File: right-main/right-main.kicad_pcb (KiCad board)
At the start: 2 copper layers, 150.4 x 123.8 mm, 208 parts, among them J1 USBCONN, P1 CONN_4, P2 CONN_5, P3 CONN_6, SW1 PTS525SM10, SW11 SPST, SW12 SPST, SW13 SPST, SW14 SPST, SW15 SPST, SW16 SPST, SW17 SPST, SW21 SPST, SW22 SPST, SW23 SPST, SW24 SPST, SW25 SPST, SW26 SPST, SW27 SPST, SW31 SPST, SW32 SPST, SW33 SPST, SW34 SPST, SW35 SPST, SW36 SPST, SW37 SPST, SW41 SPST, SW42 SPST, SW43 SPST, SW44 SPST, SW45 SPST, SW46 SPST, SW47 SPST, SW52 SPST, SW53 SPST, SW54 SPST, SW55 SPST, SW56 SPST, SW57 SPST, U1 ATMEGA32U4, U2 CAT24C256, X1 16Mhz

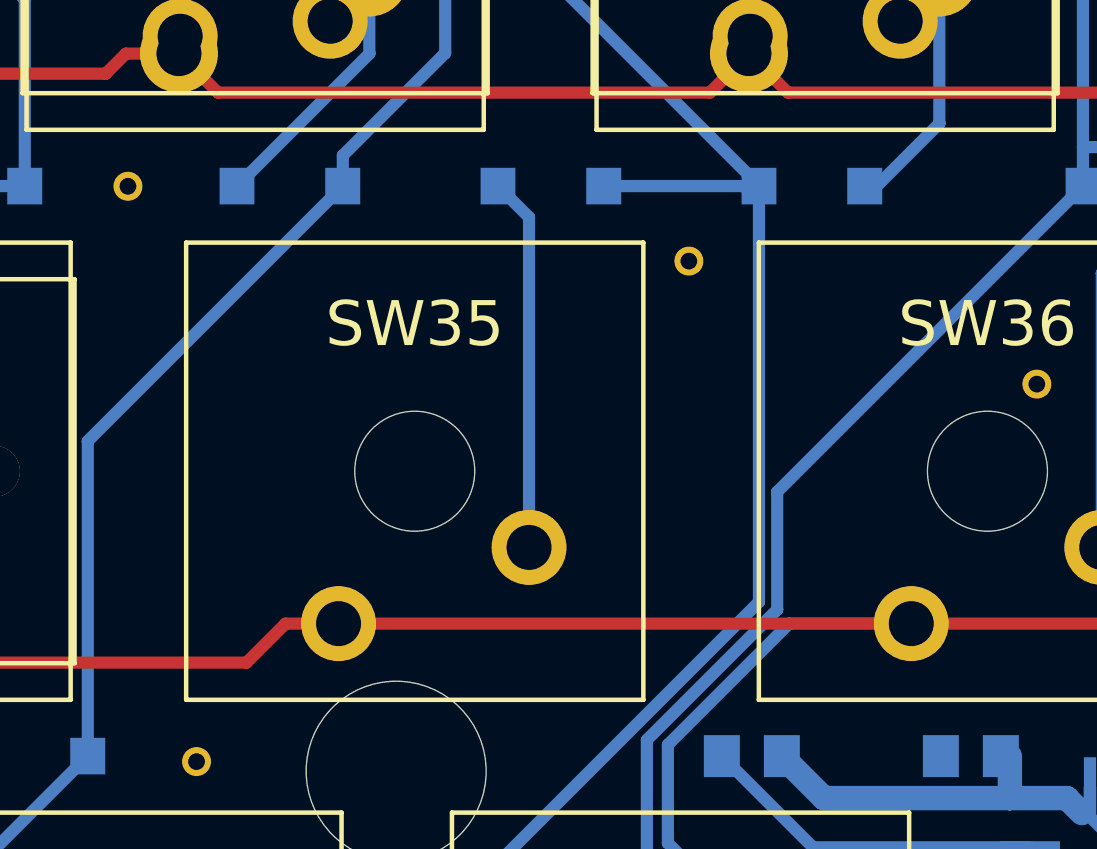
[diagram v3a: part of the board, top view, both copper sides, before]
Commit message: switch 35 right
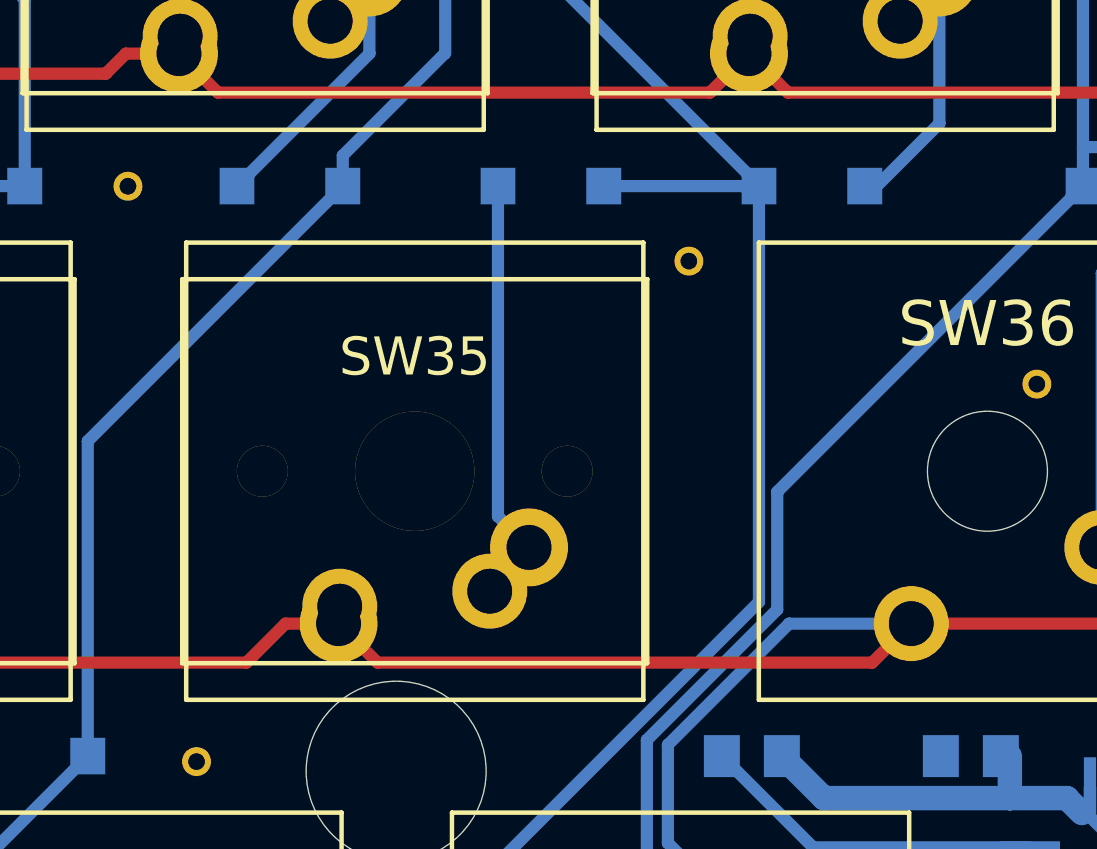
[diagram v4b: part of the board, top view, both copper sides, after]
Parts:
- SW35: footprint UGL:Cherry_MX -> ugl:Cherry-MX-Matias-Hybrid
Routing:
- net Net-(D35-Pad2): track 13.5 -> 15.5 mm
- net /ROW3: track 190.5 -> 191.6 mm
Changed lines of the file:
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@@
 (kicad_pcb (version 4) (host pcbnew 4.0.1-stable)
   (general
-    (links 345)
-    (no_connects 3)
+    (links 347)
+    (no_connects 0)
     (area 19.803 18.9051 270.000001 165.000001)
     (thickness 1.6)
     (drawings 354)
-    (tracks 1050)
+    (tracks 1054)
     (zones 0)
     (modules 208)
@@
   (layers
     (0 F.Cu signal)
-    (31 B.Cu signal hide)
+    (31 B.Cu signal)
     (32 B.Adhes user)
     (33 F.Adhes user)
@@
       (net 18 /ROW3))
   )
-  (module UGL:Cherry_MX locked (layer F.Cu)
-    (at 197.52 101.7 180)
-    (fp_text reference SW35 (at 0 4.9 180) (layer F.SilkS)
-      (effects (font (size 1.5 1.5) (thickness 0.3)))
-    )
-    (fp_text value SPST (at 0 0 180) (layer F.SilkS) hide
-      (effects (font (size 1.5 1.5) (thickness 0.3)))
-    )
-    (fp_line (start -7.6 -7.6) (end -7.6 7.6) (layer B.SilkS) (width 0.15))
-    (fp_line (start -7.6 7.6) (end 7.6 7.6) (layer B.SilkS) (width 0.15))
-    (fp_line (start 7.6 -7.6) (end 7.6 7.6) (layer B.SilkS) (width 0.15))
-    (fp_line (start -7.6 -7.6) (end 7.6 -7.6) (layer B.SilkS) (width 0.15))
-    (fp_line (start -7.62 -7.62) (end 7.62 -7.62) (layer F.SilkS) (width 0.15))
-    (fp_line (start 7.62 -7.62) (end 7.62 7.62) (layer F.SilkS) (width 0.15))
-    (fp_line (start 7.62 7.62) (end -7.62 7.62) (layer F.SilkS) (width 0.15))
-    (fp_line (start -7.62 7.62) (end -7.62 -7.62) (layer F.SilkS) (width 0.15))
-    (pad "" np_thru_hole circle (at 0 0 180) (size 4 4) (drill 4) (layers *.Cu *.Mask F.SilkS))
-    (pad 2 thru_hole circle (at -3.81 -2.54 180) (size 2.5 2.5) (drill 1.5) (layers *.Cu *.Mask F.SilkS)
-      (net 48 "Net-(D35-Pad2)"))
-    (pad 1 thru_hole circle (at 2.54 -5.08 180) (size 2.5 2.5) (drill 1.5) (layers *.Cu *.Mask F.SilkS)
-      (net 18 /ROW3))
-  )
   (module UGL:UX60-MB-5S8 locked (layer F.Cu)
     (at 175.849803 43.601924 85.4)
@@
     )
   )
+  (module ugl:Cherry-MX-Matias-Hybrid locked (layer F.Cu)
+    (at 197.52 101.7 180)
+    (tags switch)
+    (fp_text reference SW35 (at 0 3.81 180) (layer F.SilkS)
+      (effects (font (thickness 0.3048)))
+    )
+    (fp_text value SPST (at 0 0 180) (layer F.SilkS) hide
+      (effects (font (thickness 0.3048)))
+    )
+    (fp_line (start -7.62 7.62) (end -7.62 -7.62) (layer B.SilkS) (width 0.15))
+    (fp_line (start 7.62 7.62) (end -7.62 7.62) (layer B.SilkS) (width 0.15))
+    (fp_line (start 7.62 -7.62) (end 7.62 7.62) (layer B.SilkS) (width 0.15))
+    (fp_line (start -7.62 -7.62) (end 7.62 -7.62) (layer B.SilkS) (width 0.15))
+    (fp_line (start -7.75 -6.4) (end -7.75 6.4) (layer F.SilkS) (width 0.15))
+    (fp_line (start 7.75 -6.4) (end 7.75 6.4) (layer F.SilkS) (width 0.15))
+    (fp_line (start -7.75 6.4) (end 7.75 6.4) (layer F.SilkS) (width 0.15))
+    (fp_line (start -7.75 -6.4) (end 7.75 -6.4) (layer F.SilkS) (width 0.15))
+    (fp_line (start -7.62 -7.62) (end 7.62 -7.62) (layer F.SilkS) (width 0.15))
+    (fp_line (start 7.62 -7.62) (end 7.62 7.62) (layer F.SilkS) (width 0.15))
+    (fp_line (start 7.62 7.62) (end -7.62 7.62) (layer F.SilkS) (width 0.15))
+    (fp_line (start -7.62 7.62) (end -7.62 -7.62) (layer F.SilkS) (width 0.15))
+    (pad 0 thru_hole circle (at 0 0 180) (size 3.98018 3.98018) (drill 3.98018) (layers *.Cu *.Mask F.SilkS))
+    (pad 1 thru_hole circle (at 2.54 -5.08 180) (size 2.6 2.6) (drill 1.5011) (layers *.Cu *.Mask F.SilkS)
+      (net 18 /ROW3))
+    (pad 2 thru_hole circle (at -3.81 -2.54 180) (size 2.6 2.6) (drill 1.5011) (layers *.Cu *.Mask F.SilkS)
+      (net 48 "Net-(D35-Pad2)"))
+    (pad "" thru_hole circle (at -5.08 0 180) (size 1.69926 1.69926) (drill 1.69926) (layers *.Cu *.Mask F.SilkS))
+    (pad "" thru_hole circle (at 5.08 0 180) (size 1.69926 1.69926) (drill 1.69926) (layers *.Cu *.Mask F.SilkS))
+    (pad 1 thru_hole circle (at 2.5 -4.5 180) (size 2.5 2.5) (drill 1.5) (layers *.Cu *.Mask F.SilkS)
+      (net 18 /ROW3))
+    (pad 2 thru_hole circle (at -2.5 -4 180) (size 2.5 2.5) (drill 1.5) (layers *.Cu *.Mask F.SilkS)
+      (net 48 "Net-(D35-Pad2)"))
+    (model cherry_mx1.wrl
+      (at (xyz 0 0 0))
+      (scale (xyz 1 1 1))
+      (rotate (xyz 0 0 0))
+    )
+  )
   (gr_line (start 120.857 138.196) (end 121.657 137.396) (angle 90) (layer B.SilkS) (width 0.2))
   (gr_line (start 124.457 148.096) (end 124.457 148.296) (angle 90) (layer B.SilkS) (width 0.2))
@@
   (segment (start 223.2279 106.862992) (end 223.2279 112.237) (width 0.4064) (layer B.Cu) (net 17))
   (segment (start 227.66 87.78) (end 230.641 87.78) (width 0.4064) (layer B.Cu) (net 17))
+  (segment (start 214.07 106.78) (end 212.770001 108.079999) (width 0.4064) (layer F.Cu) (net 18))
+  (segment (start 212.770001 108.079999) (end 196.279999 108.079999) (width 0.4064) (layer F.Cu) (net 18))
+  (segment (start 196.279999 108.079999) (end 194.98 106.78) (width 0.4064) (layer F.Cu) (net 18))
   (segment (start 194.98 106.78) (end 193.212234 106.78) (width 0.4064) (layer F.Cu) (net 18))
   (segment (start 191.912235 108.079999) (end 177.190002 108.079999) (width 0.4064) (layer F.Cu) (net 18))
@@
   (segment (start 246.26 104.24) (end 247.303 105.283) (width 0.4064) (layer B.Cu) (net 18))
   (segment (start 247.303 105.283) (end 247.303 111.2) (width 0.4064) (layer B.Cu) (net 18))
-  (segment (start 214.07 106.78) (end 194.98 106.78) (width 0.4064) (layer F.Cu) (net 18))
   (segment (start 246.1641 104.3359) (end 246.26 104.24) (width 0.4064) (layer B.Cu) (net 18))
   (segment (start 209.997216 106.78) (end 205.957 110.820216) (width 0.4064) (layer B.Cu) (net 18))
@@
   (segment (start 183.0937 105.093697) (end 183.0937 111.196) (width 0.4064) (layer B.Cu) (net 47))
   (segment (start 182.240003 104.24) (end 183.0937 105.093697) (width 0.4064) (layer B.Cu) (net 47))
+  (segment (start 200.02 105.7) (end 200.02 105.55) (width 0.4064) (layer B.Cu) (net 48))
+  (segment (start 200.02 105.55) (end 201.33 104.24) (width 0.4064) (layer B.Cu) (net 48))
+  (segment (start 200.2937 92.196) (end 200.2937 103.2037) (width 0.4064) (layer B.Cu) (net 48))
+  (segment (start 200.2937 103.2037) (end 201.33 104.24) (width 0.4064) (layer B.Cu) (net 48))
   (segment (start 201.33 105.2291) (end 201.33 104.24) (width 0.4064) (layer B.Cu) (net 48))
-  (segment (start 201.33 93.2323) (end 201.33 104.24) (width 0.4064) (layer B.Cu) (net 48))
-  (segment (start 200.2937 92.196) (end 201.33 93.2323) (width 0.4064) (layer B.Cu) (net 48))
   (segment (start 220.42 95.0963) (end 220.42 104.24) (width 0.4064) (layer B.Cu) (net 49))
   (segment (start 223.3203 92.196) (end 220.42 95.0963) (width 0.4064) (layer B.Cu) (net 49))

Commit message: switch 36 right
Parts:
- SW36: footprint UGL:Cherry_MX -> ugl:Cherry-MX-Matias-Hybrid
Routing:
- net Net-(D36-Pad2): track 13.2 -> 15.8 mm
- net /COL6: track 100.5 -> 101.1 mm

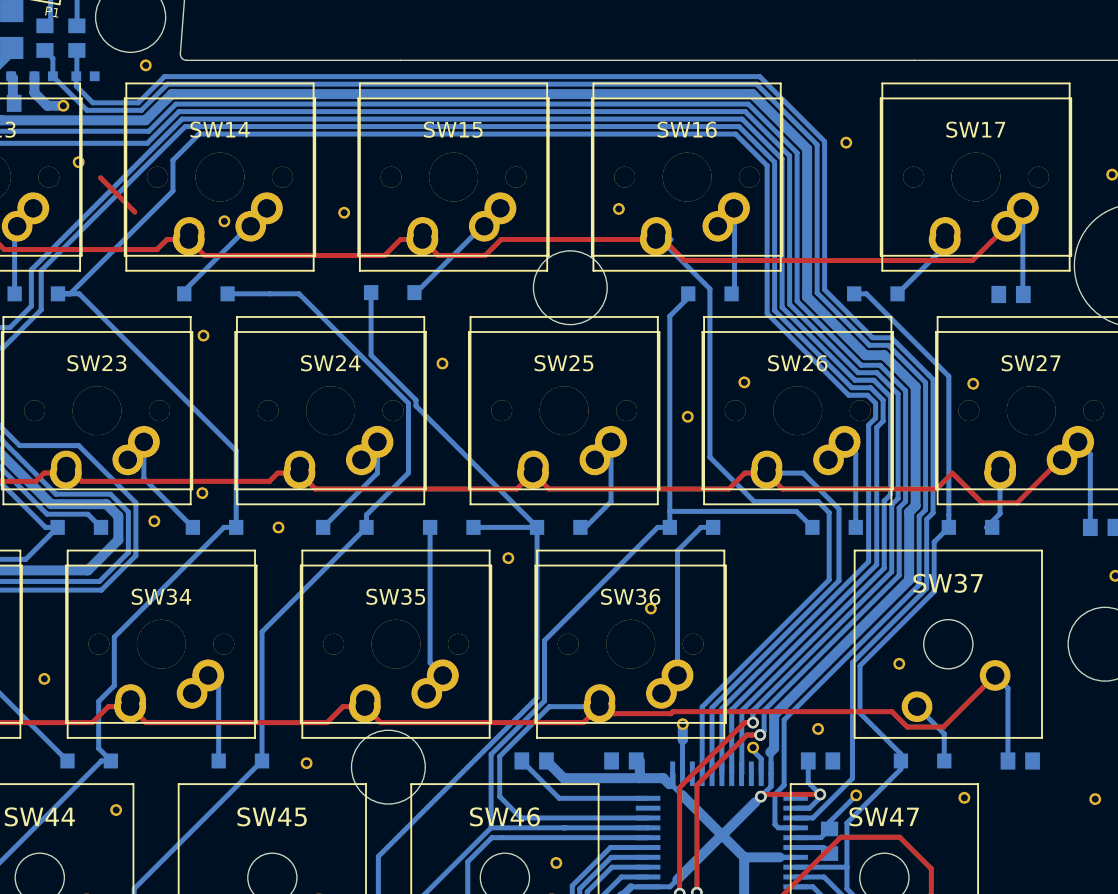
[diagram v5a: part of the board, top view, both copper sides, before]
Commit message: switch 37 right
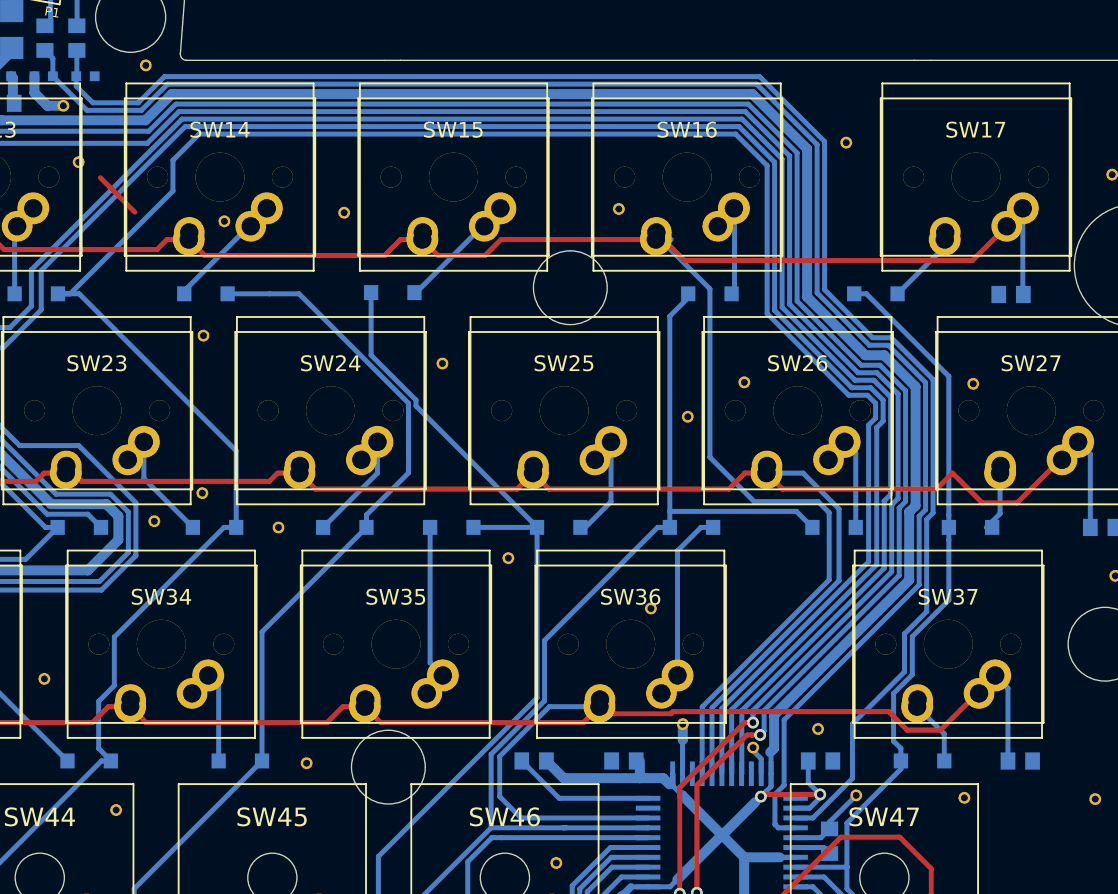
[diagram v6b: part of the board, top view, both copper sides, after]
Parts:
- SW37: footprint UGL:Cherry_MX -> ugl:Cherry-MX-Matias-Hybrid
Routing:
- net /COL7: track 88.2 -> 86.5 mm

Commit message: switch 42 right
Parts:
- SW42: footprint UGL:Cherry_MX -> ugl:Cherry-MX-Matias-Hybrid
- moved via 38/22mil 1.18 mm to (130.7, 124.5)
- moved via 38/22mil 0.57 mm to (134.4, 119.4)
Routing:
- net Net-(D42-Pad2): track 16.0 -> 18.0 mm
- net /ROW4: track 216.7 -> 217.5 mm
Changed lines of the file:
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@@
 (kicad_pcb (version 4) (host pcbnew 4.0.1-stable)
   (general
-    (links 350)
-    (no_connects 0)
+    (links 352)
+    (no_connects 1)
     (area 19.803 18.9051 270.000001 165.000001)
     (thickness 1.6)
     (drawings 354)
-    (tracks 1066)
+    (tracks 1071)
     (zones 0)
     (modules 208)
@@
   )
   (layers
-    (0 F.Cu signal hide)
-    (31 B.Cu signal)
+    (0 F.Cu signal)
+    (31 B.Cu signal hide)
     (32 B.Adhes user)
     (33 F.Adhes user)
@@
   )
   (module UGL:via_38_22mil (layer F.Cu)
-    (at 131.857 124.396)
+    (at 130.683 124.46)
     (fp_text reference "via 38/22mil" (at 0 -1.8) (layer F.SilkS) hide
       (effects (font (size 0.75 0.75) (thickness 0.15)))
@@
   )
   (module UGL:via_38_22mil (layer F.Cu)
-    (at 134.62 119.888)
+    (at 134.366 119.38)
     (fp_text reference "via 38/22mil" (at 0 -1.8) (layer F.SilkS) hide
       (effects (font (size 0.75 0.75) (thickness 0.15)))
@@
       (net 19 /ROW4))
   )
-  (module UGL:Cherry_MX locked (layer F.Cu)
-    (at 130.7 120.7 180)
-    (fp_text reference SW42 (at 0 4.9 180) (layer F.SilkS)
-      (effects (font (size 1.5 1.5) (thickness 0.3)))
-    )
-    (fp_text value SPST (at 0 0 180) (layer F.SilkS) hide
-      (effects (font (size 1.5 1.5) (thickness 0.3)))
-    )
-    (fp_line (start -7.6 -7.6) (end -7.6 7.6) (layer B.SilkS) (width 0.15))
-    (fp_line (start -7.6 7.6) (end 7.6 7.6) (layer B.SilkS) (width 0.15))
-    (fp_line (start 7.6 -7.6) (end 7.6 7.6) (layer B.SilkS) (width 0.15))
-    (fp_line (start -7.6 -7.6) (end 7.6 -7.6) (layer B.SilkS) (width 0.15))
-    (fp_line (start -7.62 -7.62) (end 7.62 -7.62) (layer F.SilkS) (width 0.15))
-    (fp_line (start 7.62 -7.62) (end 7.62 7.62) (layer F.SilkS) (width 0.15))
-    (fp_line (start 7.62 7.62) (end -7.62 7.62) (layer F.SilkS) (width 0.15))
-    (fp_line (start -7.62 7.62) (end -7.62 -7.62) (layer F.SilkS) (width 0.15))
-    (pad "" np_thru_hole circle (at 0 0 180) (size 4 4) (drill 4) (layers *.Cu *.Mask F.SilkS))
-    (pad 2 thru_hole circle (at -3.81 -2.54 180) (size 2.5 2.5) (drill 1.5) (layers *.Cu *.Mask F.SilkS)
-      (net 52 "Net-(D42-Pad2)"))
-    (pad 1 thru_hole circle (at 2.54 -5.08 180) (size 2.5 2.5) (drill 1.5) (layers *.Cu *.Mask F.SilkS)
-      (net 19 /ROW4))
-  )
   (module UGL:UX60-MB-5S8 locked (layer F.Cu)
     (at 175.849803 43.601924 85.4)
@@
     )
   )
+  (module ugl:Cherry-MX-Matias-Hybrid locked (layer F.Cu)
+    (at 130.7 120.7 180)
+    (tags switch)
+    (fp_text reference SW42 (at 0 3.81 180) (layer F.SilkS)
+      (effects (font (thickness 0.3048)))
+    )
+    (fp_text value SPST (at 0 0 180) (layer F.SilkS) hide
+      (effects (font (thickness 0.3048)))
+    )
+    (fp_line (start -7.62 7.62) (end -7.62 -7.62) (layer B.SilkS) (width 0.15))
+    (fp_line (start 7.62 7.62) (end -7.62 7.62) (layer B.SilkS) (width 0.15))
+    (fp_line (start 7.62 -7.62) (end 7.62 7.62) (layer B.SilkS) (width 0.15))
+    (fp_line (start -7.62 -7.62) (end 7.62 -7.62) (layer B.SilkS) (width 0.15))
+    (fp_line (start -7.75 -6.4) (end -7.75 6.4) (layer F.SilkS) (width 0.15))
+    (fp_line (start 7.75 -6.4) (end 7.75 6.4) (layer F.SilkS) (width 0.15))
+    (fp_line (start -7.75 6.4) (end 7.75 6.4) (layer F.SilkS) (width 0.15))
+    (fp_line (start -7.75 -6.4) (end 7.75 -6.4) (layer F.SilkS) (width 0.15))
+    (fp_line (start -7.62 -7.62) (end 7.62 -7.62) (layer F.SilkS) (width 0.15))
+    (fp_line (start 7.62 -7.62) (end 7.62 7.62) (layer F.SilkS) (width 0.15))
+    (fp_line (start 7.62 7.62) (end -7.62 7.62) (layer F.SilkS) (width 0.15))
+    (fp_line (start -7.62 7.62) (end -7.62 -7.62) (layer F.SilkS) (width 0.15))
+    (pad 0 thru_hole circle (at 0 0 180) (size 3.98018 3.98018) (drill 3.98018) (layers *.Cu *.Mask F.SilkS))
+    (pad 1 thru_hole circle (at 2.54 -5.08 180) (size 2.6 2.6) (drill 1.5011) (layers *.Cu *.Mask F.SilkS)
+      (net 19 /ROW4))
+    (pad 2 thru_hole circle (at -3.81 -2.54 180) (size 2.6 2.6) (drill 1.5011) (layers *.Cu *.Mask F.SilkS)
+      (net 52 "Net-(D42-Pad2)"))
+    (pad "" thru_hole circle (at -5.08 0 180) (size 1.69926 1.69926) (drill 1.69926) (layers *.Cu *.Mask F.SilkS))
+    (pad "" thru_hole circle (at 5.08 0 180) (size 1.69926 1.69926) (drill 1.69926) (layers *.Cu *.Mask F.SilkS))
+    (pad 1 thru_hole circle (at 2.5 -4.5 180) (size 2.5 2.5) (drill 1.5) (layers *.Cu *.Mask F.SilkS)
+      (net 19 /ROW4))
+    (pad 2 thru_hole circle (at -2.5 -4 180) (size 2.5 2.5) (drill 1.5) (layers *.Cu *.Mask F.SilkS)
+      (net 52 "Net-(D42-Pad2)"))
+    (model cherry_mx1.wrl
+      (at (xyz 0 0 0))
+      (scale (xyz 1 1 1))
+      (rotate (xyz 0 0 0))
+    )
+  )
   (gr_line (start 120.857 138.196) (end 121.657 137.396) (angle 90) (layer B.SilkS) (width 0.2))
   (gr_line (start 124.457 148.096) (end 124.457 148.296) (angle 90) (layer B.SilkS) (width 0.2))
@@
   (segment (start 207.6977 115.8367) (end 218.028 115.8367) (width 0.4064) (layer B.Cu) (net 18))
   (segment (start 214.07 106.78) (end 209.997216 106.78) (width 0.4064) (layer B.Cu) (net 18))
+  (segment (start 147.08 125.78) (end 145.312234 125.78) (width 0.4064) (layer F.Cu) (net 19))
+  (segment (start 145.312234 125.78) (end 144.012235 127.079999) (width 0.4064) (layer F.Cu) (net 19))
+  (segment (start 144.012235 127.079999) (end 129.459999 127.079999) (width 0.4064) (layer F.Cu) (net 19))
+  (segment (start 129.459999 127.079999) (end 128.16 125.78) (width 0.4064) (layer F.Cu) (net 19))
   (segment (start 128.16 125.78) (end 127.2032 124.8232) (width 0.4064) (layer F.Cu) (net 19))
   (segment (start 127.2032 124.8232) (end 127.2032 118.364) (width 0.4064) (layer F.Cu) (net 19))
@@
   (segment (start 185.759998 125.78) (end 166.560002 125.78) (width 0.4064) (layer F.Cu) (net 19))
   (segment (start 166.560002 125.78) (end 147.359997 125.78) (width 0.4064) (layer F.Cu) (net 19))
-  (segment (start 147.359997 125.78) (end 128.16 125.78) (width 0.4064) (layer F.Cu) (net 19))
   (segment (start 218.028 117.4369) (end 217.064617 117.4369) (width 0.4064) (layer B.Cu) (net 19))
   (segment (start 206.103 117.4369) (end 218.028 117.4369) (width 0.4064) (layer B.Cu) (net 19))
@@
   (segment (start 123.660007 105.55) (end 124.970007 104.24) (width 0.4064) (layer B.Cu) (net 51))
   (segment (start 164.4203 92.196) (end 162.5203 94.096) (width 0.4064) (layer B.Cu) (net 51))
+  (segment (start 133.2 124.7) (end 133.2 124.55) (width 0.4064) (layer B.Cu) (net 52) (status C00000))
+  (segment (start 133.2 124.55) (end 134.51 123.24) (width 0.4064) (layer B.Cu) (net 52) (status C00000))
   (segment (start 134.5293 123.2593) (end 134.51 123.24) (width 0.4064) (layer B.Cu) (net 52))
   (segment (start 140.3377 123.24) (end 134.51 123.24) (width 0.4064) (layer B.Cu) (net 52))
